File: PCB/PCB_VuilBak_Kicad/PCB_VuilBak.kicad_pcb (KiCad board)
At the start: 2 copper layers, 99.9 x 64.2 mm, 39 parts, among them Q1 2N7002, Q2 2N7002, U1 micro_usb, U2 AMS1117-3.3, U3 TCA9548A_I2C_Multiplexer, U4 esp_wroom_32, X1 DG3XX-04-3.5, X10 DG3XX-04-3.5, X11 DG3XX-02-3.5, X12 DG3XX-02-3.5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

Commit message: update pcb
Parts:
- added C8: 10u, Capacitor_SMD:C_0805_2012Metric, B.Cu at (348.5, 25.1)
- added R9: 10k, Capacitor_SMD:C_0805_2012Metric, B.Cu at (342.9, 73.1)
- C2, C4, C6, C7, R7: moved to B.Cu
- Q1, Q2: value 2N7002 -> BSS138
- R13: moved to F.Cu
- S1, S2: footprint 1-1825910-4:TE_1-1825910-4 -> knop:TE_1-1825910-4; moved to B.Cu
- U1: value micro_usb -> micro; footprint micro_usb:GCT_USB3090-XX-X_REVE -> micro_usb_2:MOLEX_105017-1001
- X7, X8, X9: value DG3XX-04-3.5 -> DG3XX-05-3.5; footprint pins:PinHeader_1x04_P2.54mm_Vertical -> pins:PinHeader_1x05_P2.54mm_Vertical
- moved X10 240.7 mm to (413.0, 82.1), turned to 180 degrees
- moved X7 240.3 mm to (398.0, 105.2)
- moved X8 238.4 mm to (381.7, 105.5)
- moved C5 238.2 mm to (361.1, 89.8)
- moved X9 237.1 mm to (365.7, 105.5)
- moved C7 236.3 mm to (346.1, 33.4), turned to 180 degrees
- moved R11 232.3 mm to (337.6, 44.5), turned to 90 degrees
- moved U2 232.1 mm to (351.1, 88.8)
- moved C6 231.8 mm to (344.8, 25.0)
- moved C4 231.0 mm to (355.7, 25.1)
- moved U1 230.6 mm to (349.2, 116.7)
- moved X12 229.9 mm to (331.3, 27.2)
- moved X13 229.8 mm to (331.2, 34.8)
- moved X4 229.7 mm to (330.6, 69.2), turned to 0 degrees
- moved X11 229.7 mm to (331.0, 42.7)
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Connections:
- C1 pad 2: 3.3V -> 5V
- R1 pad 2: 3.3V -> 5V
- R2 pad 2: 3.3V -> 5V
- U3 pad 24: 3.3V -> 5V
- U3 pad 3: unconnected-(U3-Pad3) -> Net-(R9-Pad2)
- X2 pad 4: 5V -> 3.3V
- X3 pad 4: 5V -> 3.3V
- X4 pad 1: 5V -> 3.3V
- X7 pad 4: GND -> GPIO 16
- X8 pad 4: GND -> GPIO4
- X9 pad 4: GND -> GPIO2
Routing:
- net GND: track 478.5 -> 656.1 mm, vias 3 -> 9
- net 3.3V: track 374.3 -> 468.0 mm, vias 7 -> 9
- net SC7: track 28.1 -> 85.5 mm, vias 0 -> 1
- net SD7: track 27.5 -> 83.4 mm, vias 0 -> 1
- net GPIO2: track 58.8 -> 103.6 mm
- net GPIO4: track 45.1 -> 86.8 mm, vias 0 -> 2
- net GPIO 16: track 44.7 -> 84.0 mm, vias 0 -> 2
- net SD5: track 45.8 -> 84.6 mm, vias 0 -> 1
- net SD6: track 36.3 -> 74.4 mm, vias 0 -> 1
- net SC6: track 35.7 -> 72.9 mm, vias 0 -> 1
- net SC5: track 46.0 -> 82.5 mm, vias 0 -> 1
- net SDA_ESP: track 37.0 -> 73.3 mm, vias 1 -> 3
- net SCL_Mux: track 76.1 -> 106.6 mm, vias 0 -> 3
- net SDA_mux: track 67.7 -> 96.8 mm, vias 2 -> 3
- net SCL_ESP: track 49.2 -> 75.1 mm, vias 1 -> 3
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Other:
- board outline removed
- board text added: "3.3V"
- board text added: "5V"
- board text added: "BOOT"
- board text added: "ENABLE"
- board text added: "GND"
- board text added: "GPIO 04"
- board text added: "GPIO 12"
- board text added: "GPIO 13"
- board text added: "GPIO 14"
- board text added: "GPIO 15"
- board text added: "GPIO 16"
- board text added: "GPIO 17"
- board text added: "GPIO 18"
- board text added: "GPIO 19"
- board text added: "GPIO 2"
- board text added: "GPIO 23"
- board text added: "GPIO 26"
- board text added: "GPIO 27"
- board text added: "GPIO 32"
- board text added: "GPIO 33"
- board text added: "GPIO 5"
- board text added: "GPIO25"
- board text added: "IRQ"
- board text added: "KEYPAD"
- board text added: "KNOP 1"
- board text added: "KNOP 2"
- board text added: "KNOP 3"
- board text added: "LCD"
- board text added: "LOAD SENSOR 1"
- board text added: "LOAD SENSOR 2"
- board text added: "LOAD SENSOR 3"
- board text added: "RFID1"
- board text added: "RFID2"
- board text added: "RFID3"
- board text added: "RX"
- board text added: "SCL"
- board text added: "SDA"
- board text added: "SPEAKER"
- board text added: "TX"
- board text added: "UART"

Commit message: update pcb
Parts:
- moved C5 202.6 mm to (158.5, 92.8)
- moved C6 202.6 mm to (142.2, 28.0)
- moved C7 202.6 mm to (143.5, 36.4)
- moved Q1 202.6 mm to (170.2, 75.9)
- moved Q2 202.6 mm to (172.8, 86.2)
- moved R11 202.6 mm to (135.0, 47.5)
- moved R13 202.6 mm to (135.0, 41.2)
- moved R2 202.6 mm to (168.1, 87.0)
- moved R4 202.6 mm to (177.8, 86.2)
- moved R5 202.6 mm to (165.5, 75.0)
- moved R6 202.6 mm to (163.8, 87.1)
- moved R9 202.6 mm to (140.2, 76.1)
- moved U1 202.6 mm to (146.6, 119.7)
- moved U2 202.6 mm to (148.5, 91.8)
- moved U4 202.6 mm to (171.3, 38.1)
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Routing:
- net 3.3V: track 468.0 -> 470.2 mm
- net GND: track 656.1 -> 657.9 mm
- net SDA_ESP: track 73.3 -> 74.7 mm
- net 5V: track 354.6 -> 355.7 mm
- net SCL_Mux: track 106.6 -> 107.4 mm
- net SDA_mux: track 96.8 -> 97.4 mm

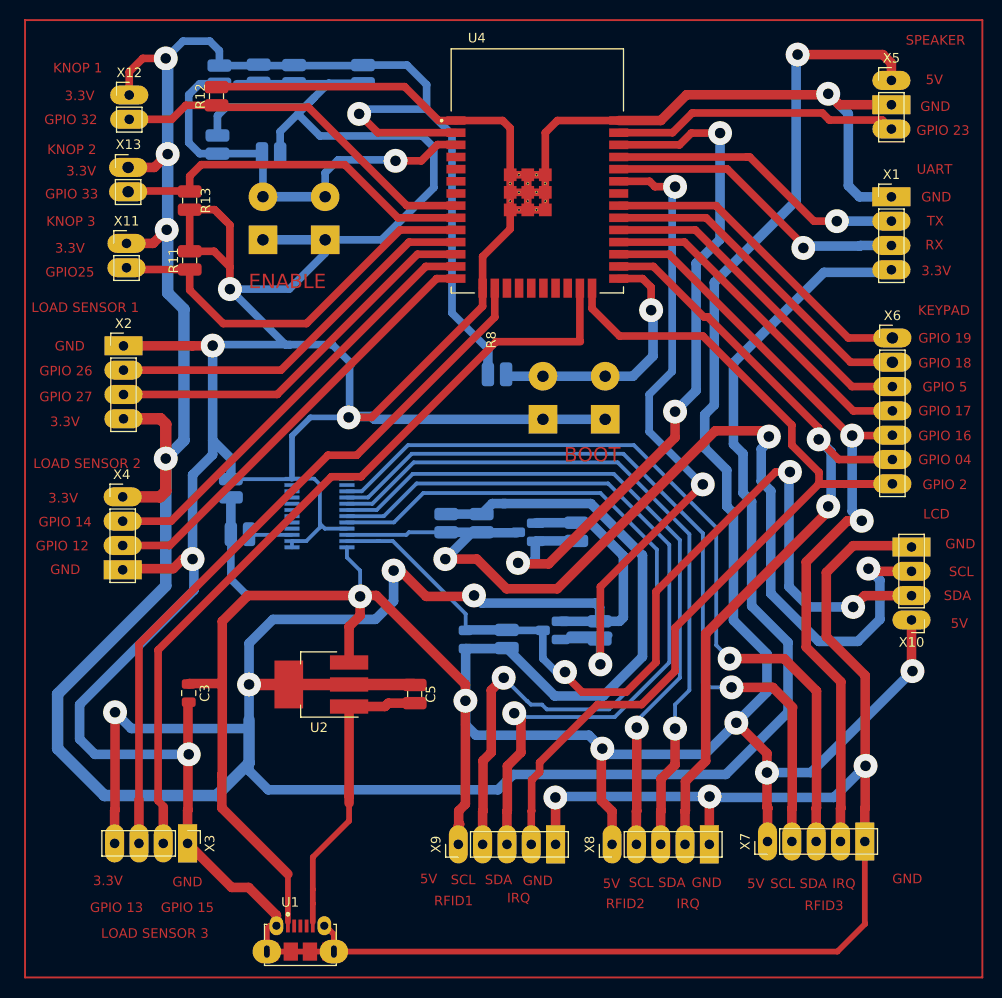
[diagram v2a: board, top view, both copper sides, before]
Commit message: Adding ground plane
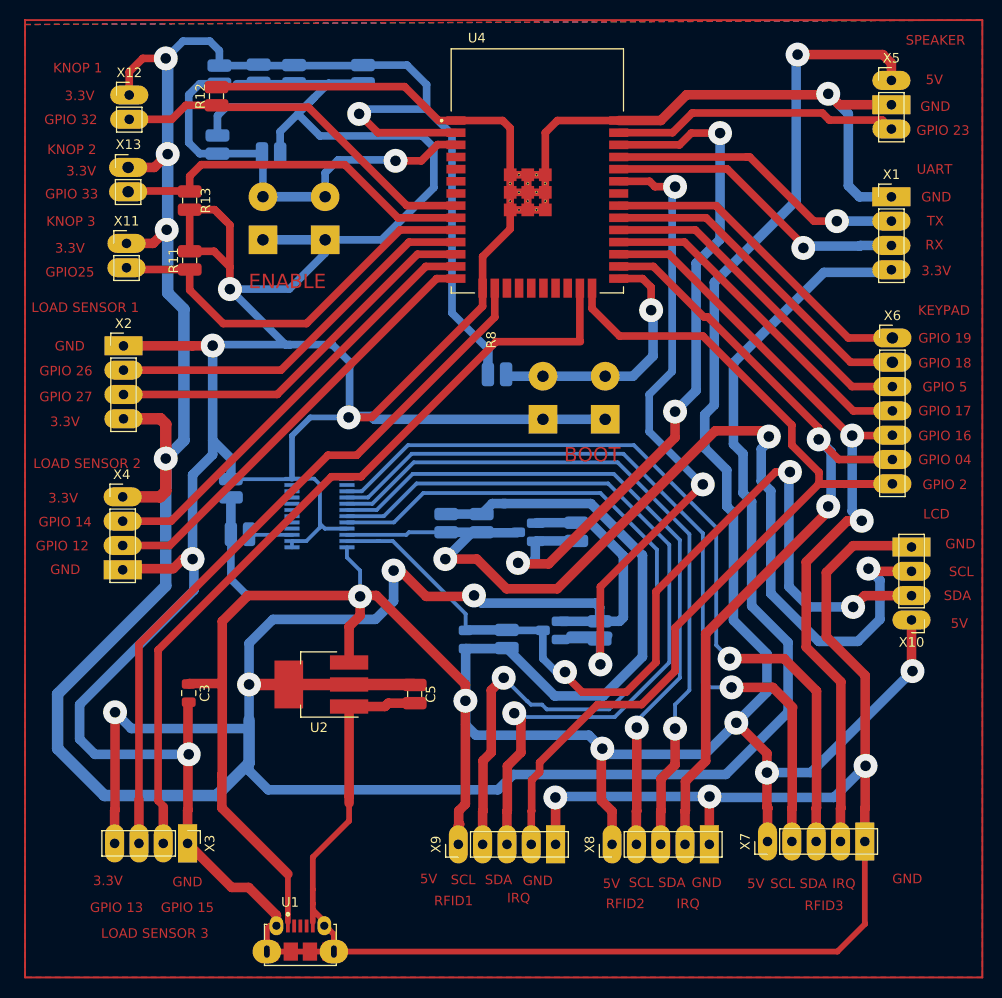
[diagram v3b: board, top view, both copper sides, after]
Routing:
- net GND: track 657.9 -> 660.0 mm
- added copper zone on B.Cu, net GND
- added copper zone on F.Cu, net GND
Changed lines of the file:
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@@
   (segment (start 168.4775 40.39) (end 168.4775 38.555) (width 0.8) (layer "F.Cu") (net 1))
   (segment (start 149.06 117) (end 149.16 117) (width 0.6) (layer "F.Cu") (net 1))
+  (segment (start 147.86 116.625) (end 147.86 115.348) (width 0.6) (layer "F.Cu") (net 1))
   (segment (start 137.9 42.5) (end 138.8 43.4) (width 0.8) (layer "F.Cu") (net 1))
   (segment (start 201.7 30.1) (end 202.84 31.24) (width 1) (layer "F.Cu") (net 1))
@@
   (segment (start 168.4775 42.225) (end 168.4775 44.2225) (width 0.8) (layer "F.Cu") (net 1))
   (segment (start 157.45 29.35) (end 160.99 32.89) (width 0.8) (layer "F.Cu") (net 1))
-  (segment (start 147.86 116.625) (end 147.86 114.7) (width 0.6) (layer "F.Cu") (net 1))
   (segment (start 145.56 119.7) (end 143.06 119.7) (width 0.6) (layer "F.Cu") (net 1))
   (segment (start 210.9 77.3) (end 204.3 77.3) (width 1) (layer "F.Cu") (net 1))
+  (segment (start 149.06 116.548) (end 149.06 117) (width 0.6) (layer "F.Cu") (net 1))
   (segment (start 150.06 119.7) (end 202.66 119.7) (width 0.6) (layer "F.Cu") (net 1))
   (segment (start 139.2 48.2) (end 139.2 43.8) (width 0.8) (layer "F.Cu") (net 1))
   (segment (start 135 42.2) (end 137.6 42.2) (width 0.8) (layer "F.Cu") (net 1))
+  (segment (start 147.86 115.348) (end 147.86 114.7) (width 0.6) (layer "F.Cu") (net 1))
   (segment (start 154 63.9) (end 151.6 63.9) (width 0.8) (layer "F.Cu") (net 1))
   (segment (start 155.75 93.75) (end 155.4 94.1) (width 1) (layer "F.Cu") (net 1))
@@
   (segment (start 135.3 78.7) (end 134.284412 78.7) (width 1) (layer "F.Cu") (net 1))
   (segment (start 205.52 104.74) (end 205.52 108.2) (width 1) (layer "F.Cu") (net 1))
+  (segment (start 147.86 115.348) (end 149.06 116.548) (width 0.6) (layer "F.Cu") (net 1))
   (segment (start 184.21 32.89) (end 179.8125 32.89) (width 1) (layer "F.Cu") (net 1))
   (segment (start 201.5 80.1) (end 201.5 86.8) (width 1) (layer "F.Cu") (net 1))
@@
   (segment (start 141.28 76.17) (end 145.685 76.17) (width 0.4) (layer "B.Cu") (net 59))
   (segment (start 141.15 76.3) (end 141.28 76.17) (width 0.4) (layer "B.Cu") (net 59))
+  (zone (net 1) (net_name "GND") (layers F&B.Cu) (hatch edge 0.508)
+    (connect_pads (clearance 0.508))
+    (min_thickness 0.254) (filled_areas_thickness no)
+    (fill yes (thermal_gap 0.508) (thermal_bridge_width 0.508))
+    (polygon
+      (pts
+        (xy 217.8 122.4)
+        (xy 117.8 122.4)
+        (xy 117.8 22.86)
+        (xy 217.8 22.4)
+      )
+    )
+  )
 )

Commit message: last check
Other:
- board outline added: 100 x 100 mm
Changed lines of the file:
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@@
     )
   )
-  (gr_rect (start 117.8 22.4) (end 217.8 122.4) (layer "F.Cu") (width 0.2) (fill none))
+  (gr_rect (start 117.8 22.4) (end 217.8 122.4) (layer "Edge.Cuts") (width 0.2) (fill none))
   (gr_text "GPIO 26" (at 122.07 59.05) (layer "F.Cu")
     (effects (font (size 1 1) (thickness 0.2)))
